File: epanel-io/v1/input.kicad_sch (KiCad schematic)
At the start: 4 parts

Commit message: ok let's go!
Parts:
- gave numbers to parts that had none: 4
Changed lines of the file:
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@@
   (symbol (lib_id "Device:R") (at 175.26 92.71 270)
     (in_bom yes) (on_board yes) (fields_autoplaced)
-    (property "Reference" "R?" (id 0) (at 175.26 87.7275 90))
+    (property "Reference" "R69" (id 0) (at 175.26 87.7275 90))
     (property "Value" "33KΩ/0.5W" (id 1) (at 175.26 90.5026 90))
     (property "Footprint" "Resistor_SMD:R_0805_2012Metric" (id 2) (at 175.26 90.932 90)
@@
   (symbol (lib_id "power:GND") (at 134.62 95.25 0)
     (in_bom yes) (on_board yes)
-    (property "Reference" "#PWR?" (id 0) (at 134.62 101.6 0)
+    (property "Reference" "#PWR038" (id 0) (at 134.62 101.6 0)
       (effects (font (size 1.27 1.27)) hide)
     )
@@
   (symbol (lib_id "power:+3V3") (at 124.46 78.74 0)
     (in_bom yes) (on_board yes) (fields_autoplaced)
-    (property "Reference" "#PWR?" (id 0) (at 124.46 82.55 0)
+    (property "Reference" "#PWR037" (id 0) (at 124.46 82.55 0)
       (effects (font (size 1.27 1.27)) hide)
     )
@@
   (symbol (lib_id "Isolator:H11AA1") (at 147.32 90.17 0) (mirror y)
     (in_bom yes) (on_board yes) (fields_autoplaced)
-    (property "Reference" "U?" (id 0) (at 147.32 82.3935 0))
+    (property "Reference" "U21" (id 0) (at 147.32 82.3935 0))
     (property "Value" "H11AA1" (id 1) (at 147.32 85.1686 0))
     (property "Footprint" "Package_DIP:SMDIP-6_W9.53mm" (id 2) (at 159.766 95.123 0)
@@
   (symbol (lib_id "Device:R") (at 124.46 85.09 180)
     (in_bom yes) (on_board yes) (fields_autoplaced)
-    (property "Reference" "R?" (id 0) (at 126.238 84.1815 0)
+    (property "Reference" "R67" (id 0) (at 126.238 84.1815 0)
       (effects (font (size 1.27 1.27)) (justify right))
     )
@@
   (symbol (lib_id "Device:R") (at 175.26 82.55 270)
     (in_bom yes) (on_board yes) (fields_autoplaced)
-    (property "Reference" "R?" (id 0) (at 175.26 77.5675 90))
+    (property "Reference" "R68" (id 0) (at 175.26 77.5675 90))
     (property "Value" "33KΩ/0.5W" (id 1) (at 175.26 80.3426 90))
     (property "Footprint" "Resistor_SMD:R_0805_2012Metric" (id 2) (at 175.26 80.772 90)

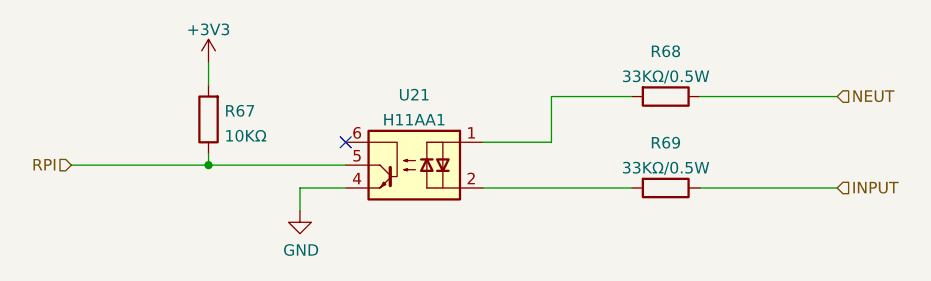
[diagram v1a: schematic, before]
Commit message: fix ZC line/neut
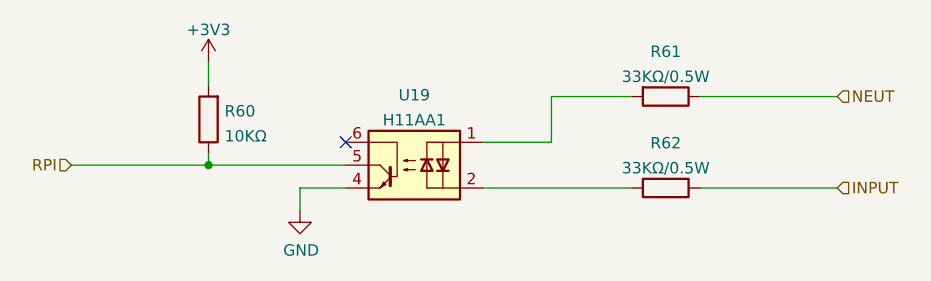
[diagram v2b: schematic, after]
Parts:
- renumbered R67 to R60, R68 to R61, R69 to R62, U21 to U19
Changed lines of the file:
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@@
   (symbol (lib_id "Device:R") (at 175.26 92.71 270)
     (in_bom yes) (on_board yes) (fields_autoplaced)
-    (property "Reference" "R69" (id 0) (at 175.26 87.7275 90))
+    (property "Reference" "R62" (id 0) (at 175.26 87.7275 90))
     (property "Value" "33KΩ/0.5W" (id 1) (at 175.26 90.5026 90))
     (property "Footprint" "Resistor_SMD:R_0805_2012Metric" (id 2) (at 175.26 90.932 90)
@@
   (symbol (lib_id "power:GND") (at 134.62 95.25 0)
     (in_bom yes) (on_board yes)
-    (property "Reference" "#PWR038" (id 0) (at 134.62 101.6 0)
+    (property "Reference" "#PWR035" (id 0) (at 134.62 101.6 0)
       (effects (font (size 1.27 1.27)) hide)
     )
@@
   (symbol (lib_id "power:+3V3") (at 124.46 78.74 0)
     (in_bom yes) (on_board yes) (fields_autoplaced)
-    (property "Reference" "#PWR037" (id 0) (at 124.46 82.55 0)
+    (property "Reference" "#PWR034" (id 0) (at 124.46 82.55 0)
       (effects (font (size 1.27 1.27)) hide)
     )
@@
   (symbol (lib_id "Isolator:H11AA1") (at 147.32 90.17 0) (mirror y)
     (in_bom yes) (on_board yes) (fields_autoplaced)
-    (property "Reference" "U21" (id 0) (at 147.32 82.3935 0))
+    (property "Reference" "U19" (id 0) (at 147.32 82.3935 0))
     (property "Value" "H11AA1" (id 1) (at 147.32 85.1686 0))
     (property "Footprint" "Package_DIP:SMDIP-6_W9.53mm" (id 2) (at 159.766 95.123 0)
@@
   (symbol (lib_id "Device:R") (at 124.46 85.09 180)
     (in_bom yes) (on_board yes) (fields_autoplaced)
-    (property "Reference" "R67" (id 0) (at 126.238 84.1815 0)
+    (property "Reference" "R60" (id 0) (at 126.238 84.1815 0)
       (effects (font (size 1.27 1.27)) (justify right))
     )
@@
   (symbol (lib_id "Device:R") (at 175.26 82.55 270)
     (in_bom yes) (on_board yes) (fields_autoplaced)
-    (property "Reference" "R68" (id 0) (at 175.26 77.5675 90))
+    (property "Reference" "R61" (id 0) (at 175.26 77.5675 90))
     (property "Value" "33KΩ/0.5W" (id 1) (at 175.26 80.3426 90))
     (property "Footprint" "Resistor_SMD:R_0805_2012Metric" (id 2) (at 175.26 80.772 90)
